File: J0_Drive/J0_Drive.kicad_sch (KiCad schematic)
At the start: 0 parts

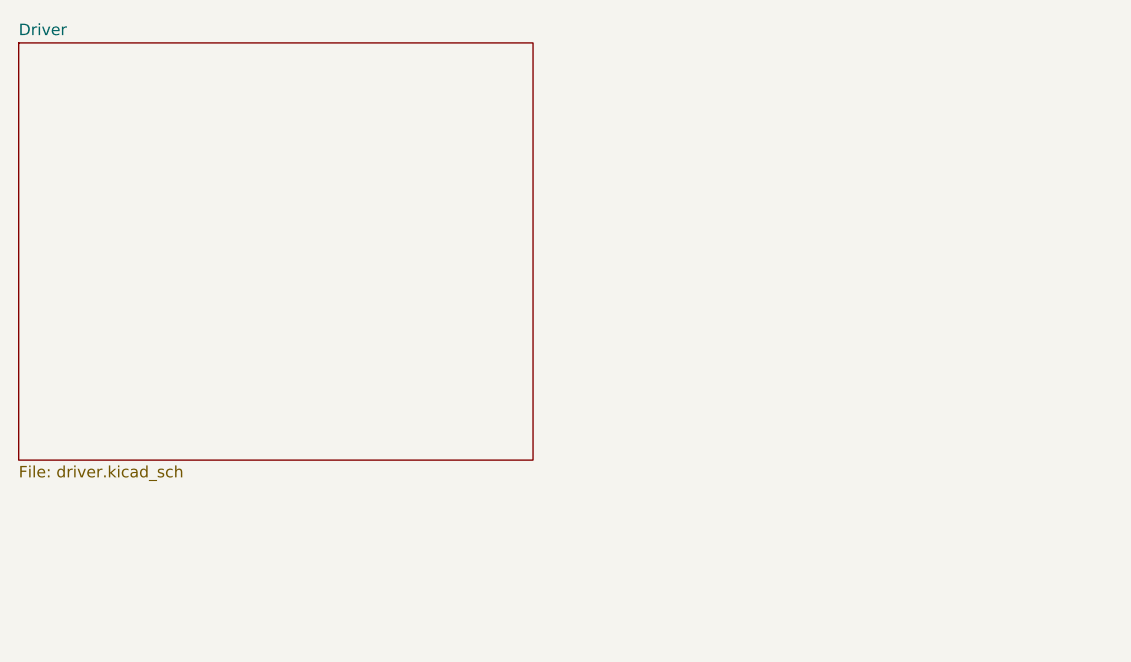
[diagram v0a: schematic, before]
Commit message: finished first design of driver page
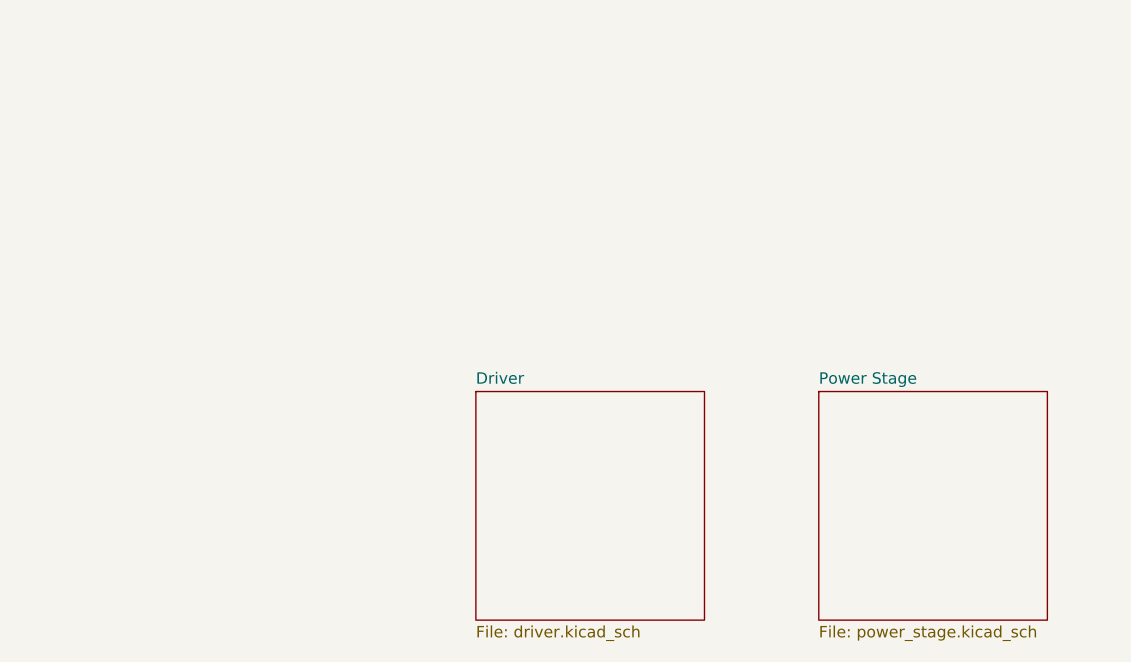
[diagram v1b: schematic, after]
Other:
- added sheet Power Stage (power_stage.kicad_sch)
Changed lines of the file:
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@@
 	(paper "A4")
 	(sheet
-		(at 76.2 50.165)
-		(size 57.15 46.355)
+		(at 127 88.9)
+		(size 25.4 25.4)
 		(exclude_from_sim no)
 		(in_bom yes)
@@
 		)
 		(property "Sheetname" "Driver"
-			(at 76.2 49.4534 0)
+			(at 127 88.1884 0)
 			(show_name no)
 			(do_not_autoplace no)
@@
 		)
 		(property "Sheetfile" "driver.kicad_sch"
-			(at 76.2 97.1046 0)
+			(at 127 114.8846 0)
 			(show_name no)
 			(do_not_autoplace no)
@@
 				)
 			)
+		)
+	)
+	(sheet
+		(at 165.1 88.9)
+		(size 25.4 25.4)
+		(exclude_from_sim no)
+		(in_bom yes)
+		(on_board yes)
+		(dnp no)
+		(fields_autoplaced yes)
+		(stroke
+			(width 0.1524)
+			(type solid)
+		)
+		(fill
+			(color 0 0 0 0)
+		)
+		(property "Sheetname" "Power Stage"
+			(at 165.1 88.1884 0)
+			(show_name no)
+			(do_not_autoplace no)
+			(effects
+				(font
+					(size 1.27 1.27)
+				)
+				(justify left bottom)
+			)
+		)
+		(property "Sheetfile" "power_stage.kicad_sch"
+			(at 165.1 114.8846 0)
+			(show_name no)
+			(do_not_autoplace no)
+			(effects
+				(font
+					(size 1.27 1.27)
+				)
+				(justify left top)
+			)
+		)
+		(instances
+			(project "J0_Drive"
+				(path "/00bb46ee-9cfb-4ad9-9820-c6d5e19a8f16"
+					(page "3")
+				)
+			)

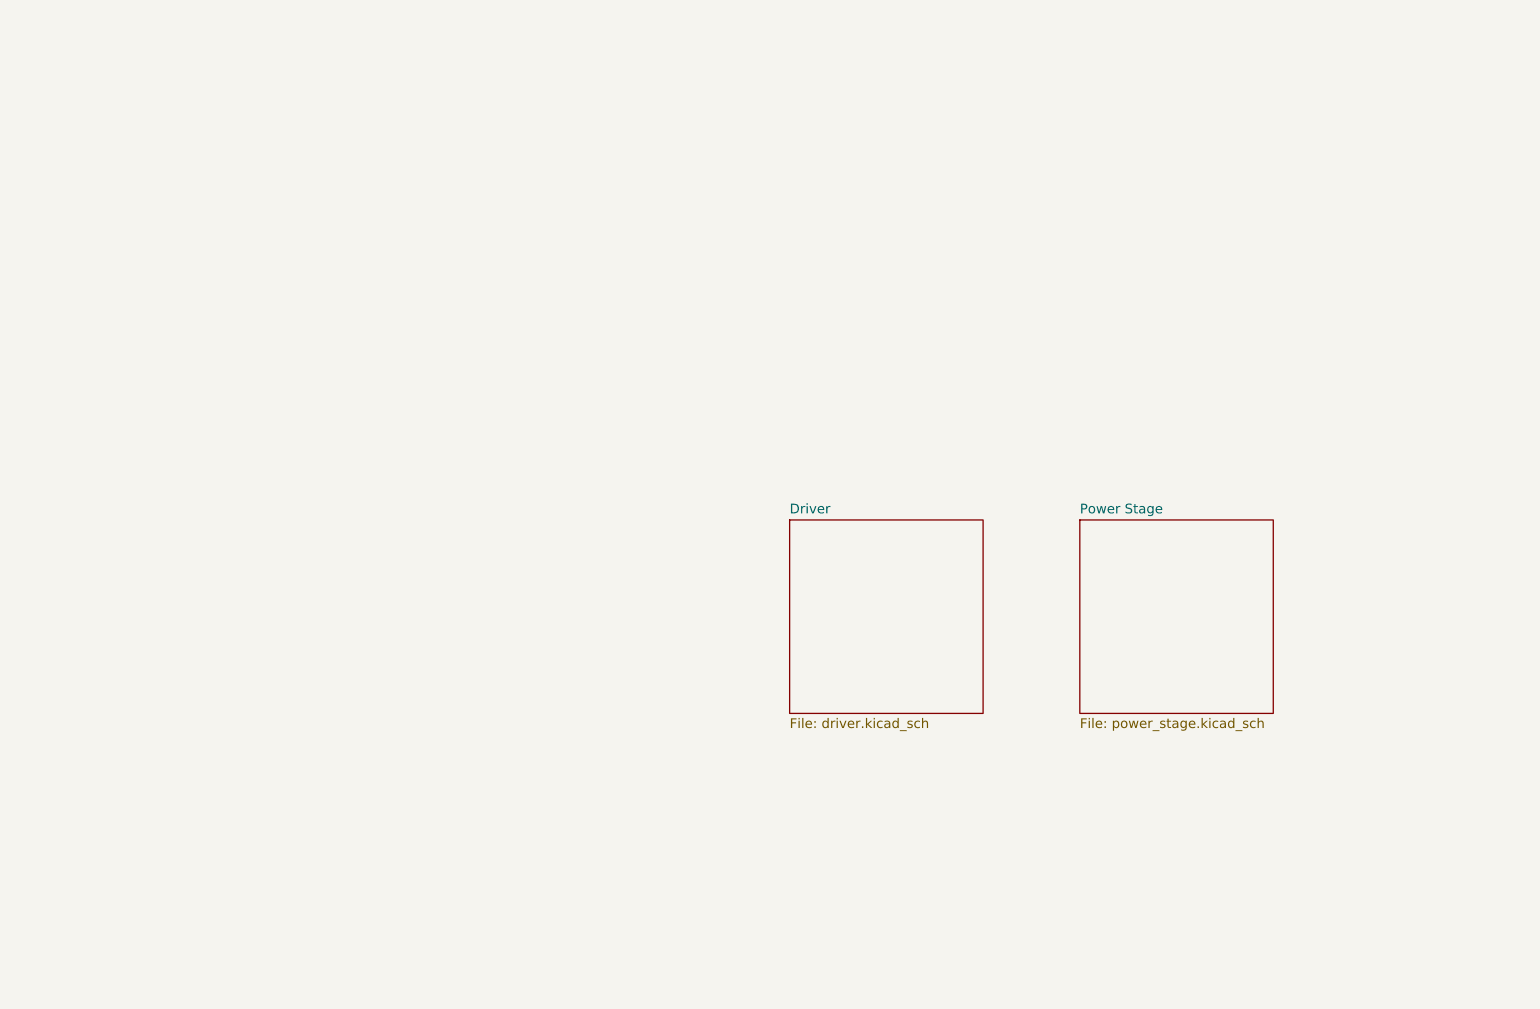
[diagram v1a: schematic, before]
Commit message: finished half bridges, started mcu
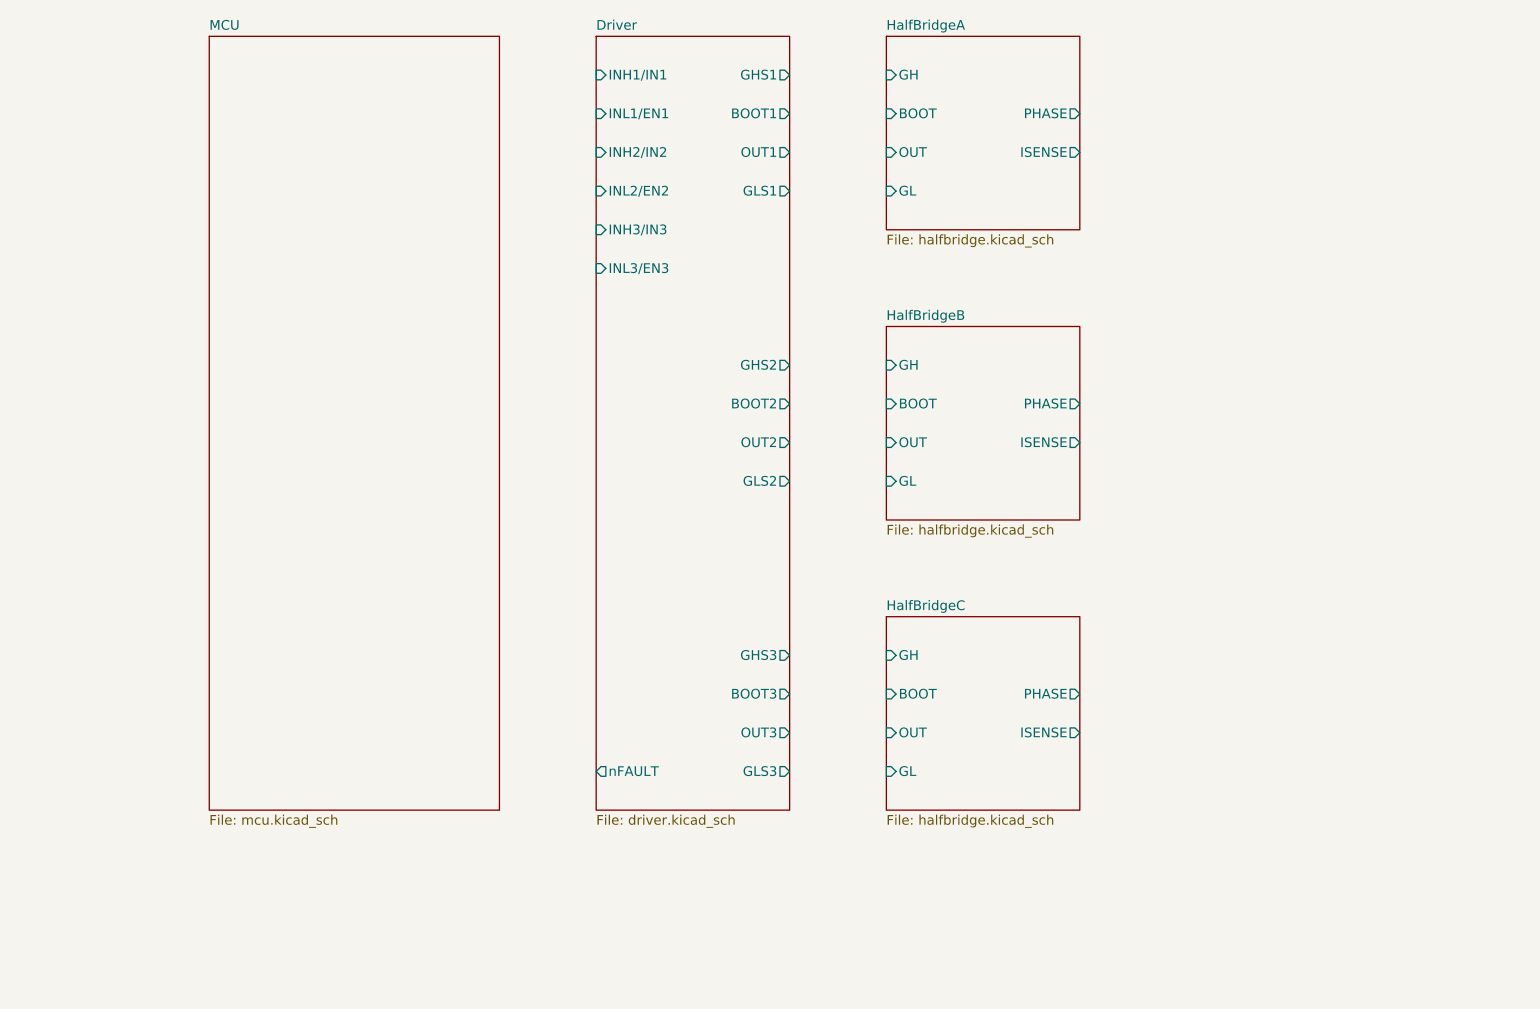
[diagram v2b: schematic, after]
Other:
- sheet Power Stage renamed HalfBridgeA
- added sheet HalfBridgeB (halfbridge.kicad_sch)
- added sheet HalfBridgeC (halfbridge.kicad_sch)
- added sheet MCU (mcu.kicad_sch)
- sheet Driver ports: added BOOT1, BOOT2, BOOT3, GHS1, GHS2, GHS3, GLS1, GLS2, GLS3, INH1/IN1, INH2/IN2, INH3/IN3, INL1/EN1, INL2/EN2, INL3/EN3, OUT1, OUT2, OUT3, nFAULT; removed none
- sheet HalfBridgeA: file power_stage.kicad_sch -> halfbridge.kicad_sch
- sheet HalfBridgeA ports: added BOOT, GH, GL, ISENSE, OUT, PHASE; removed none

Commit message: started connecting root
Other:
- sheet MCU ports: added INH1/IN1, INH2/IN2, INH3/IN3, INL1/EN1, INL2/EN2, INL3/EN3, ISENSE_A, ISENSE_B, ISENSE_C, nFAULT; removed none

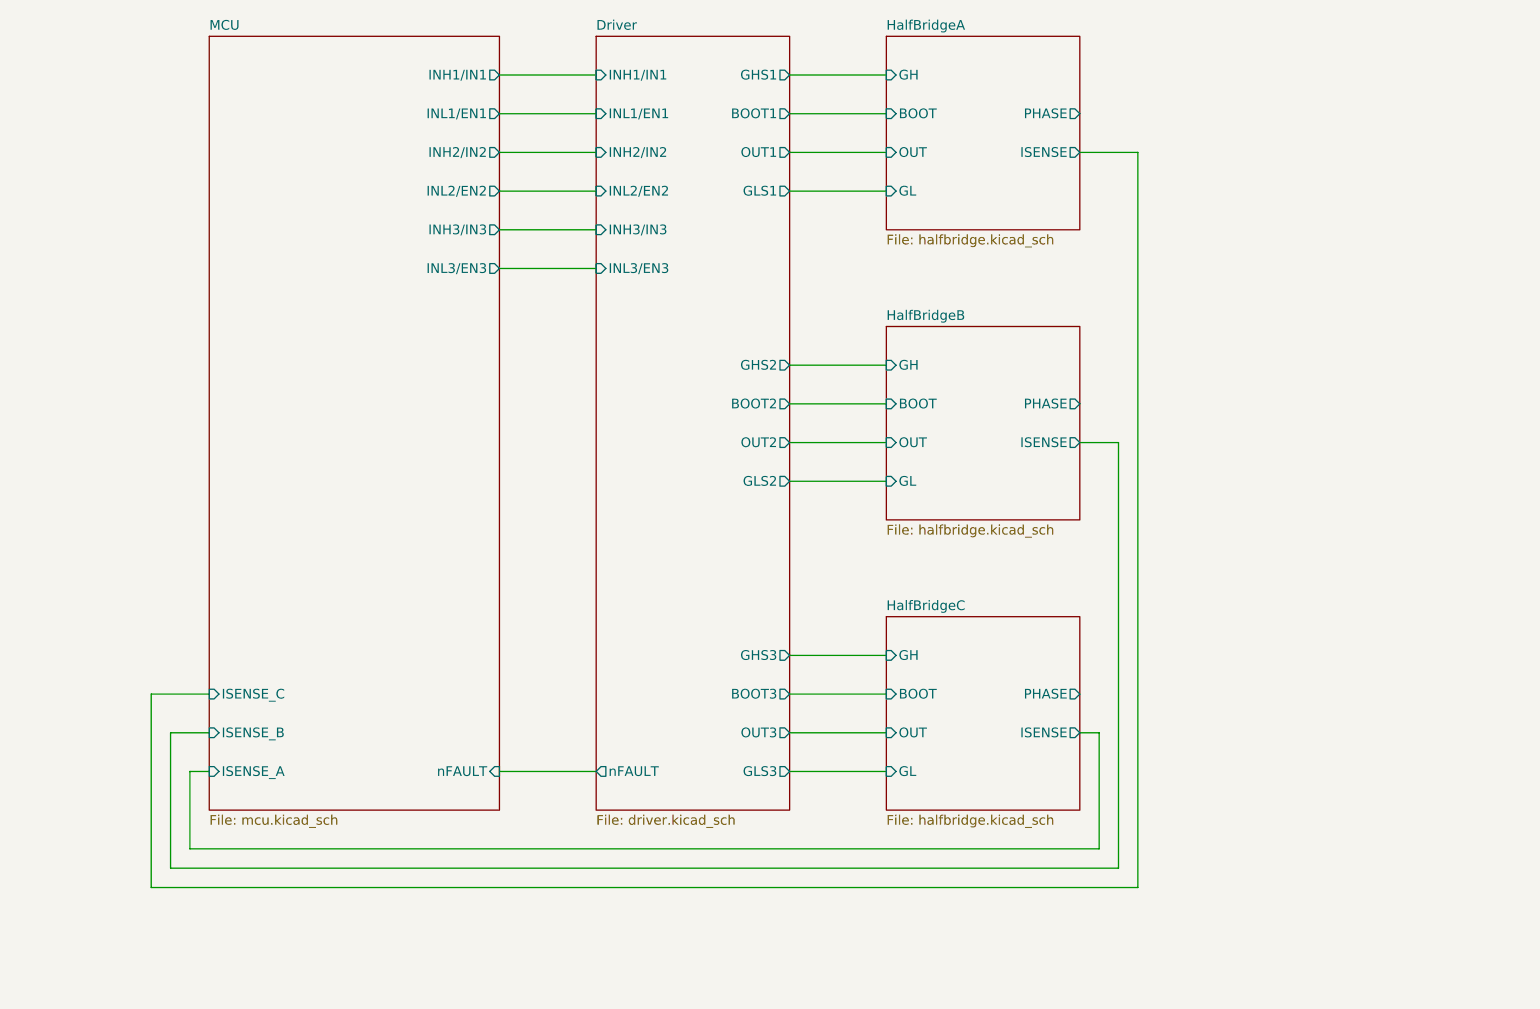
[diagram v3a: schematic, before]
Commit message: added CAN and SWD
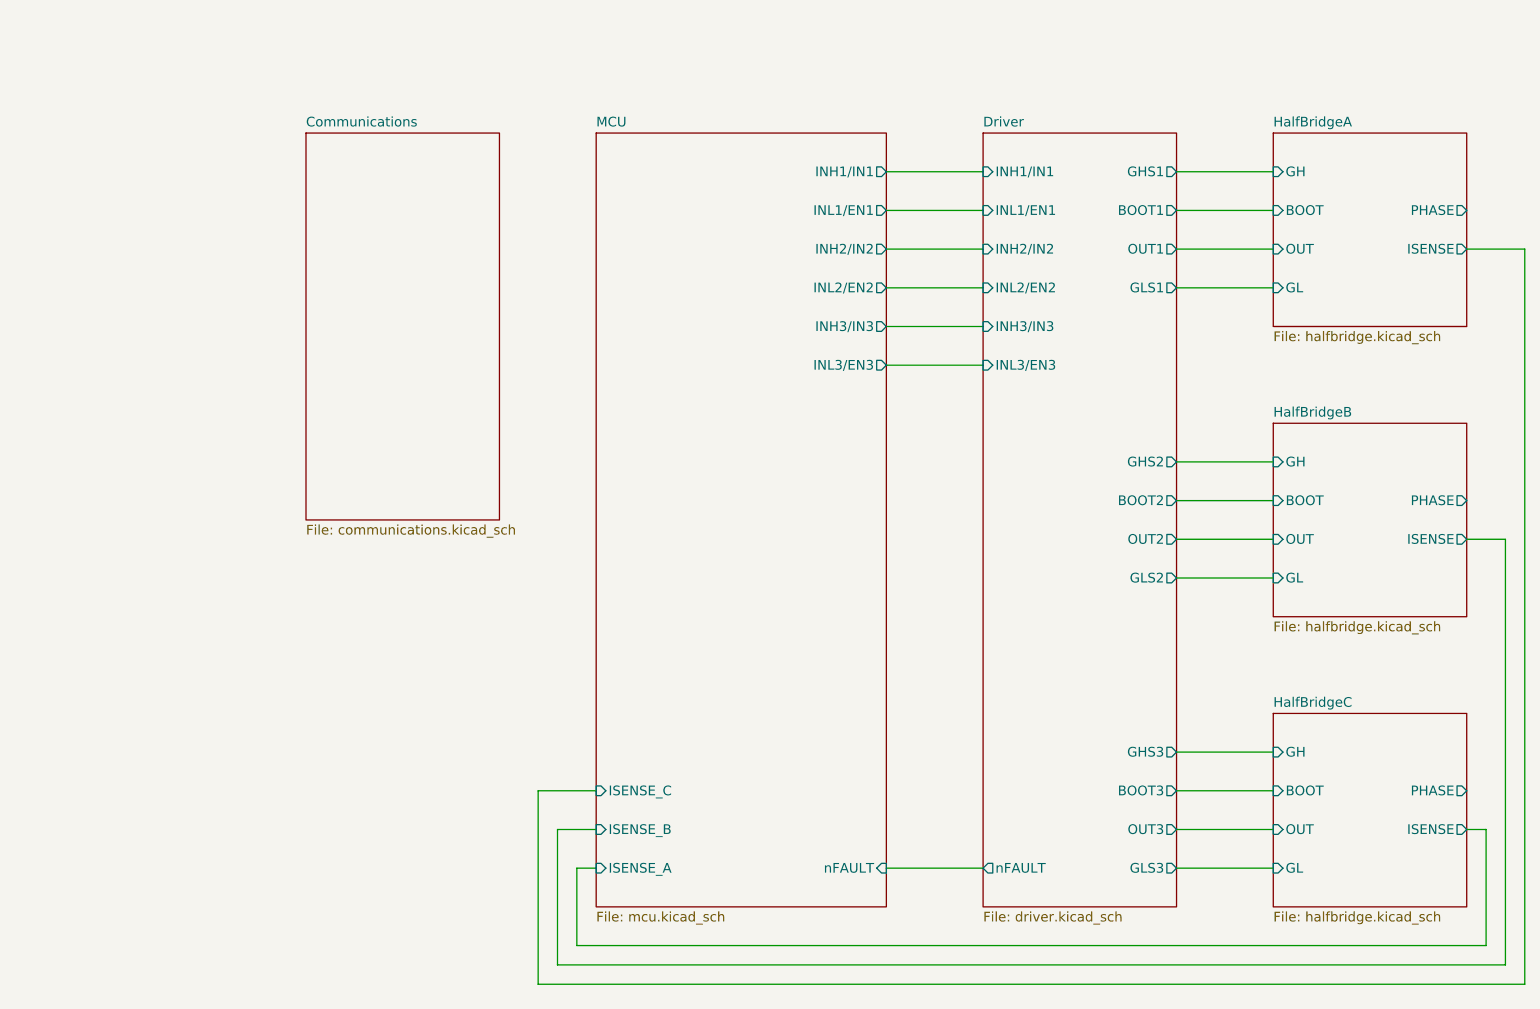
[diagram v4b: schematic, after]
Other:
- added sheet Communications (communications.kicad_sch)

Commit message: organized hierarchical sheets, finished communications, started sensors
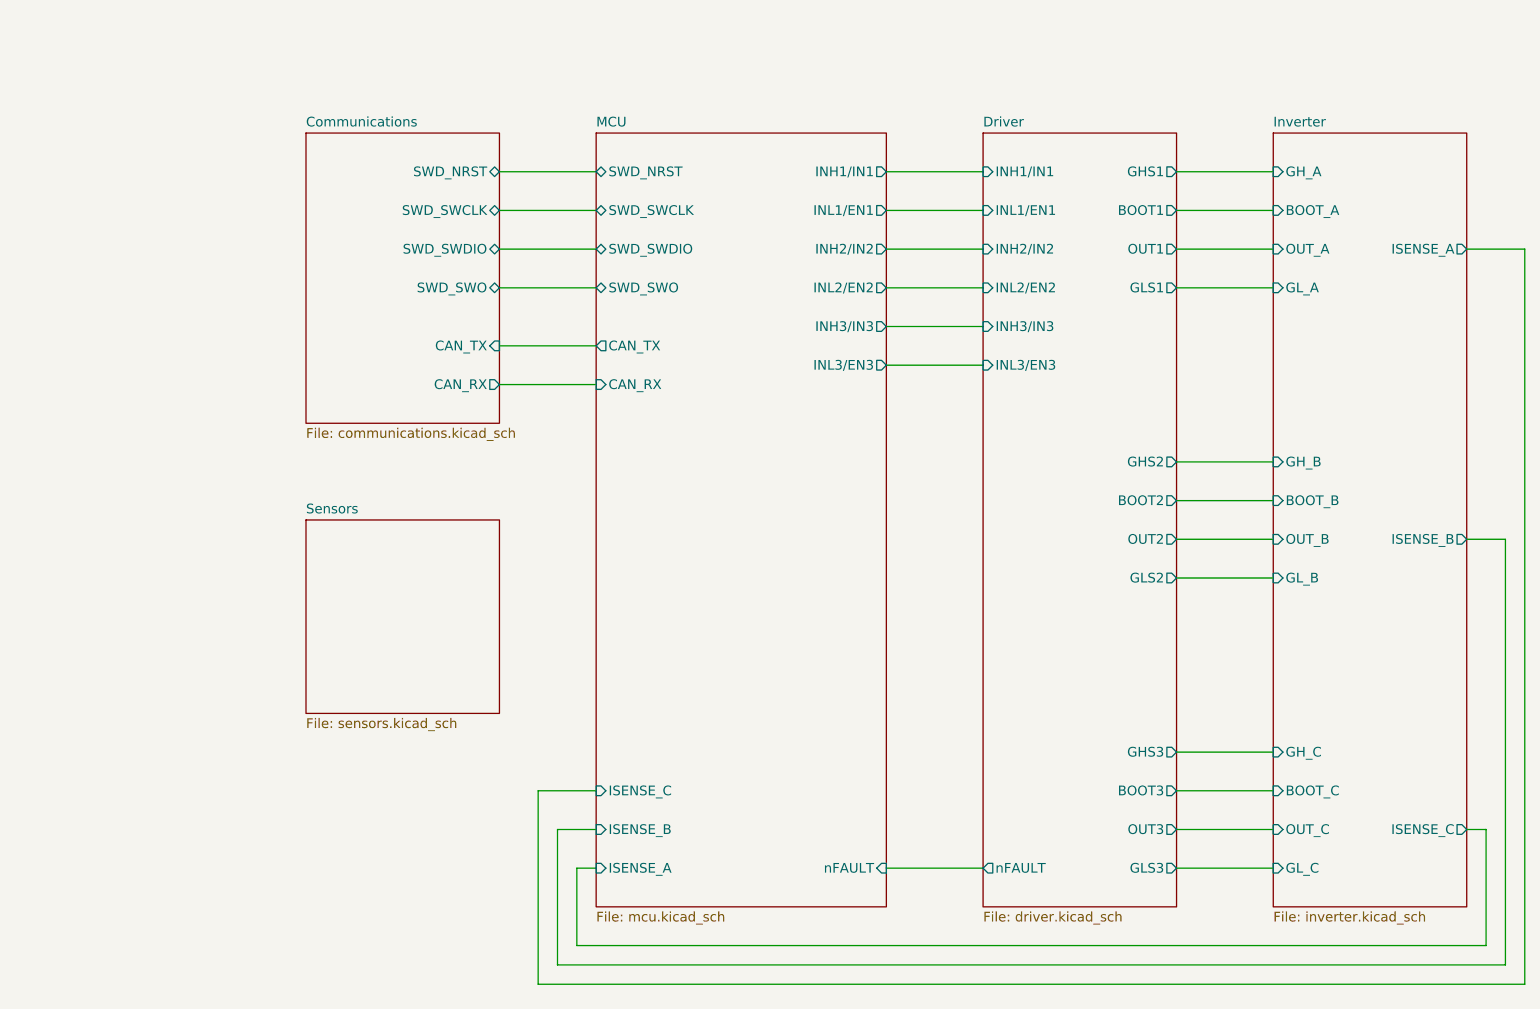
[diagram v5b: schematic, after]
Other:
- removed sheet HalfBridgeA
- removed sheet HalfBridgeB
- removed sheet HalfBridgeC
- added sheet Inverter (inverter.kicad_sch)
- added sheet Sensors (sensors.kicad_sch)
- sheet Communications ports: added CAN_RX, CAN_TX, SWD_NRST, SWD_SWCLK, SWD_SWDIO, SWD_SWO; removed none
- sheet MCU ports: added CAN_RX, CAN_TX, SWD_NRST, SWD_SWCLK, SWD_SWDIO, SWD_SWO; removed none

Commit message: finished comms SWD header, main page organization
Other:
- sheet Sensors ports: added ENC_A, ENC_B, ENC_CLK, ENC_I/PWM, ENC_MISO, ENC_MOSI, ENC_U, ENC_V, ENC_W/PWM, ENC_nCS; removed none
